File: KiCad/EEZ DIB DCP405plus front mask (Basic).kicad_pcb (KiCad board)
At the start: 2 copper layers, 35.4 x 111.5 mm, 7 parts

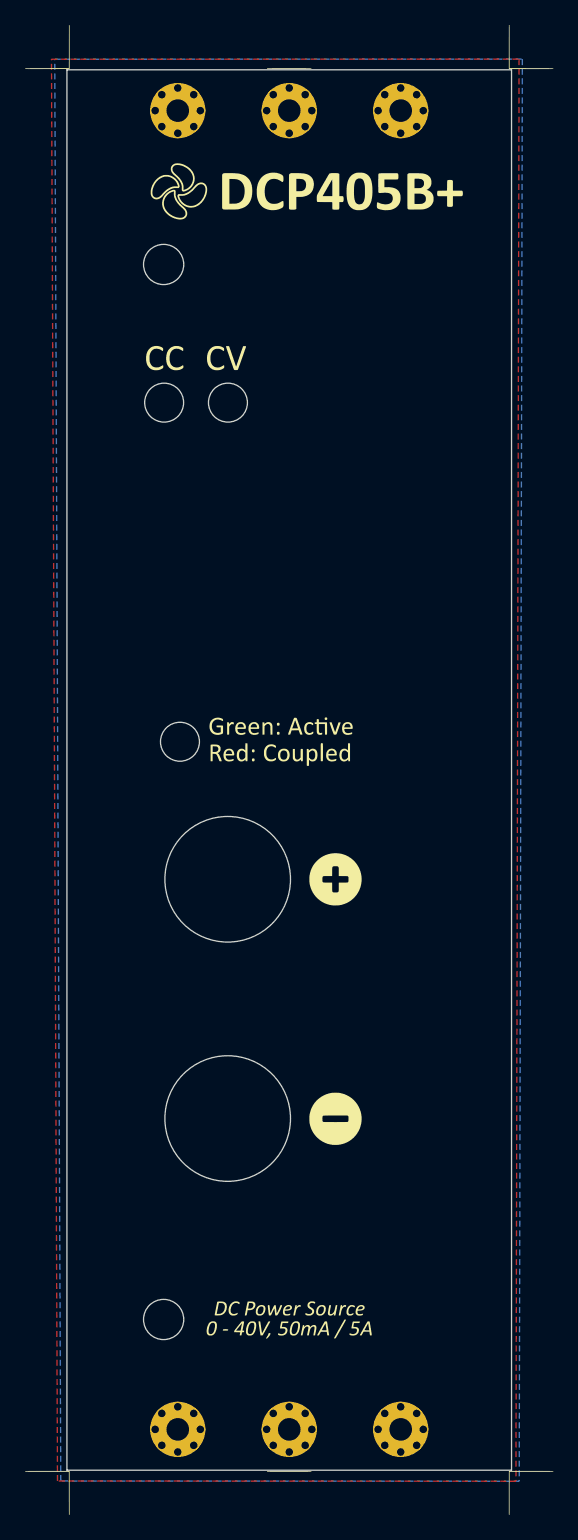
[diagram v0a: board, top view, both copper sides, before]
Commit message: Front masks added into main schematics
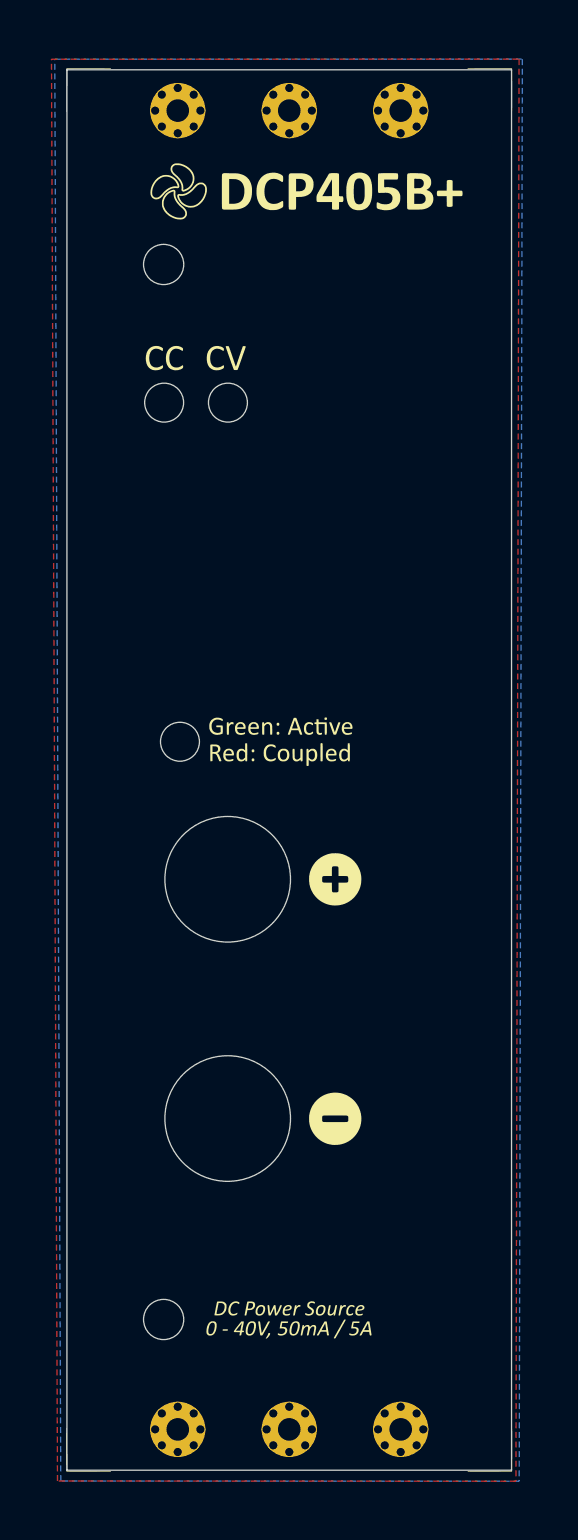
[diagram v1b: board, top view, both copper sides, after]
